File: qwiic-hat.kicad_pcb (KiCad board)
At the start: 2 copper layers, 16.2 x 65 mm, 5 parts, among them J1 Conn_02x20_Odd_Even, J2 Conn_01x04_Male, J3 Conn_01x04_Male

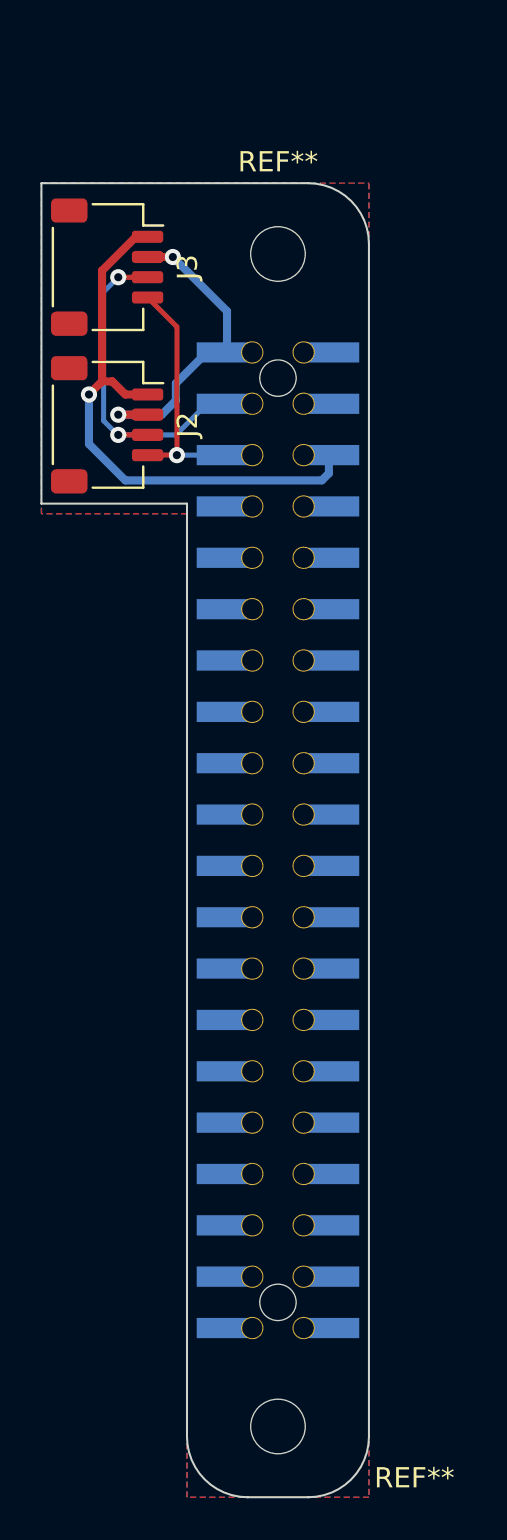
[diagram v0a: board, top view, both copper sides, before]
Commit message: added a 5v 3-pin header
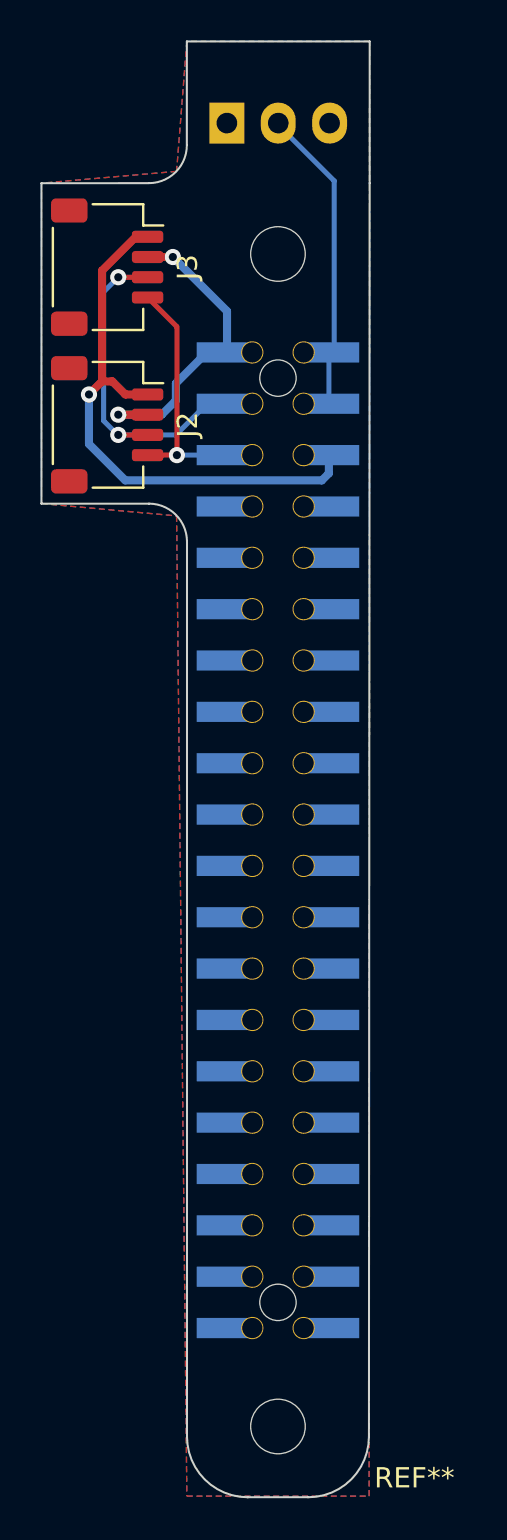
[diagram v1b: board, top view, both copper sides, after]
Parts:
- added J4: Conn_01x03_Pin, Connector:FanPinHeader_1x03_P2.54mm_Vertical, B.Cu at (173.0, 63.5)
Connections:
- J1 pad 2: unconnected-(J1-Pad2) -> +5V
- J1 pad 33: unconnected-(J1-Pad33) -> PWM1
- J1 pad 4: unconnected-(J1-Pad4) -> +5V
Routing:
- net +5V: track 0.00 -> 15.1 mm
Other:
- board size 16.2 x 65 mm -> 16.2 x 72 mm
- board text added: "carlossless.io"
